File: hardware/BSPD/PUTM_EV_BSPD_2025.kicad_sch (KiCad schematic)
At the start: 37 parts, among them J1 BS2, J2 BS1, J3 CS, K2 TE AXICOM IM07DTS, Q1 BS170F, U10 LM393B, U11 74HC1G08GV, U5 74HC1G08GV, U6 74HC3G14, U8 NE555DR

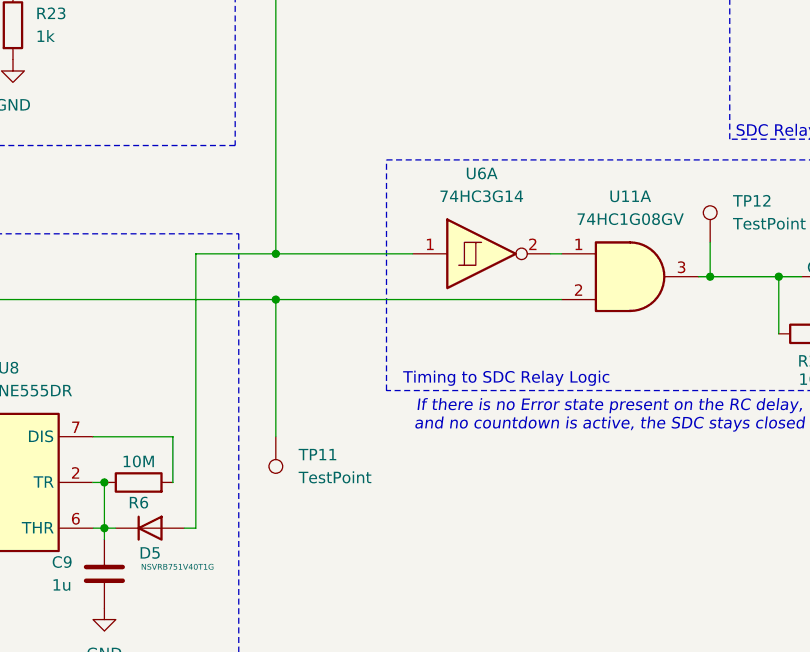
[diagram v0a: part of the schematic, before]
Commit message: Minor changes + reassigned inverters
Inverters changed to 2 dual packaged, since one more inverter appeared, and there was no quad inverter from chosen series.
Placed TestPoints more sensically
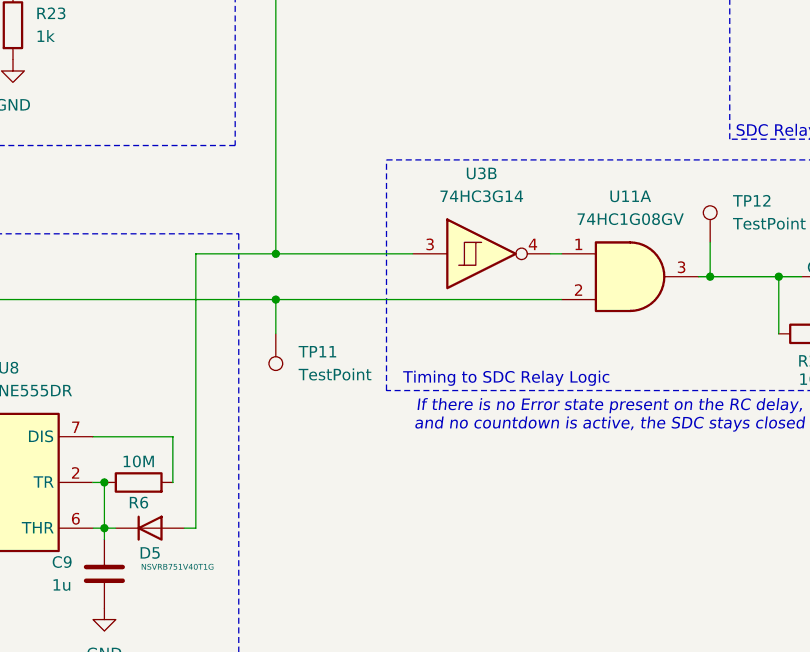
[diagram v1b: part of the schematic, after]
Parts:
- renumbered U6 to U3
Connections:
- net at D5.2 (A), R4.2, TP10.1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: now also U3.3; no longer U3.1
- net at U11.1: now also U3.4; no longer U3.2
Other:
- moved on the sheet: TP11
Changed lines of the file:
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@@
 	(wire
 		(pts
-			(xy 173.99 116.84) (xy 173.99 101.6)
+			(xy 173.99 105.41) (xy 173.99 101.6)
 		)
 		(stroke
@@
 		(lib_id "74xx:74HC14")
 		(at 196.85 96.52 0)
-		(unit 1)
+		(unit 2)
 		(exclude_from_sim no)
 		(in_bom yes)
@@
 		(dnp no)
 		(fields_autoplaced yes)
-		(property "Reference" "U6"
+		(property "Reference" "U3"
 			(at 196.85 87.63 0)
 			(effects
@@
 			(project ""
 				(path "/b652b05a-4e3d-4ad1-b032-18886abe7d45"
-					(reference "U6")
-					(unit 1)
+					(reference "U3")
+					(unit 2)
 				)
 			)
@@
 	(symbol
 		(lib_id "Connector:TestPoint")
-		(at 173.99 116.84 180)
+		(at 173.99 105.41 180)
 		(unit 1)
 		(exclude_from_sim no)
@@
 		(fields_autoplaced yes)
 		(property "Reference" "TP11"
-			(at 176.53 118.8719 0)
+			(at 176.53 107.4419 0)
 			(effects
 				(font
@@
 		)
 		(property "Value" "TestPoint"
-			(at 176.53 121.4119 0)
+			(at 176.53 109.9819 0)
 			(effects
 				(font
@@
 		)
 		(property "Footprint" ""
-			(at 168.91 116.84 0)
+			(at 168.91 105.41 0)
 			(effects
 				(font
@@
 		)
 		(property "Datasheet" "~"
-			(at 168.91 116.84 0)
+			(at 168.91 105.41 0)
 			(effects
 				(font
@@
 		)
 		(property "Description" "test point"
-			(at 173.99 116.84 0)
+			(at 173.99 105.41 0)
 			(effects
 				(font

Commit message: Assigned footprints
Harwin connectors not yet assigned!
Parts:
- C16, C17, C18, C7, C8, C9: footprint (none) -> Capacitor_SMD:C_0603_1608Metric
- D1: footprint (none) -> Diode_SMD:D_SMA
- D5: footprint (none) -> Diode_SMD:D_SOD-323_HandSoldering
- Q1: footprint (none) -> Package_TO_SOT_SMD:SOT-23
- R18, R19, R20, R22, R23, R4, R6: footprint (none) -> Resistor_SMD:R_0603_1608Metric
- U10: footprint (none) -> Package_SO:VSSOP-8_3x3mm_P0.65mm
- U11, U5: footprint (none) -> Package_TO_SOT_SMD:SOT-23-5
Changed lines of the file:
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@@
 			)
 		)
-		(property "Footprint" ""
+		(property "Footprint" "Resistor_SMD:R_0603_1608Metric"
 			(at 143.002 52.07 90)
 			(effects
@@
 			)
 		)
-		(property "Footprint" ""
+		(property "Footprint" "Resistor_SMD:R_0603_1608Metric"
 			(at 233.68 107.188 90)
 			(effects
@@
 			)
 		)
-		(property "Footprint" ""
+		(property "Footprint" "Capacitor_SMD:C_0603_1608Metric"
 			(at 82.55 177.8 0)
 			(effects
@@
 			)
 		)
-		(property "Footprint" ""
+		(property "Footprint" "Resistor_SMD:R_0603_1608Metric"
 			(at 143.002 71.12 90)
 			(effects
@@
 			)
 		)
-		(property "Footprint" ""
+		(property "Footprint" "Resistor_SMD:R_0603_1608Metric"
 			(at 134.112 66.04 90)
 			(effects
@@
 			)
 		)
-		(property "Footprint" ""
+		(property "Footprint" "Resistor_SMD:R_0603_1608Metric"
 			(at 116.84 61.468 90)
 			(effects
@@
 			)
 		)
-		(property "Footprint" ""
+		(property "Footprint" "Capacitor_SMD:C_0603_1608Metric"
 			(at 155.9052 135.89 0)
 			(effects
@@
 			)
 		)
-		(property "Footprint" ""
+		(property "Footprint" "Diode_SMD:D_SOD-323_HandSoldering"
 			(at 160.02 127 0)
 			(effects
@@
 			)
 		)
-		(property "Footprint" ""
+		(property "Footprint" "Package_SO:VSSOP-8_3x3mm_P0.65mm"
 			(at 156.21 62.23 0)
 			(effects
@@
 			)
 		)
-		(property "Footprint" ""
+		(property "Footprint" "Package_SO:VSSOP-8_3x3mm_P0.65mm"
 			(at 66.04 176.53 0)
 			(effects
@@
 			)
 		)
-		(property "Footprint" ""
+		(property "Footprint" "Resistor_SMD:R_0603_1608Metric"
 			(at 158.75 123.698 90)
 			(effects
@@
 			)
 		)
-		(property "Footprint" ""
+		(property "Footprint" "Resistor_SMD:R_0603_1608Metric"
 			(at 172.212 52.07 90)
 			(effects
@@
 			)
 		)
-		(property "Footprint" ""
+		(property "Footprint" "Package_TO_SOT_SMD:SOT-23"
 			(at 242.57 96.52 0)
 			(effects
@@
 			)
 		)
-		(property "Footprint" ""
+		(property "Footprint" "Package_TO_SOT_SMD:SOT-23-5"
 			(at 213.36 99.06 0)
 			(effects
@@
 			)
 		)
-		(property "Footprint" ""
+		(property "Footprint" "Package_TO_SOT_SMD:SOT-23-5"
 			(at 34.29 176.53 0)
 			(effects
@@
 			)
 		)
-		(property "Footprint" ""
+		(property "Footprint" "Package_TO_SOT_SMD:SOT-23-5"
 			(at 80.01 96.52 0)
 			(effects
@@
 			)
 		)
-		(property "Footprint" ""
+		(property "Footprint" "Package_TO_SOT_SMD:SOT-23-5"
 			(at 90.17 177.8 0)
 			(effects
@@
 			)
 		)
-		(property "Footprint" ""
+		(property "Footprint" "Capacitor_SMD:C_0603_1608Metric"
 			(at 68.58 176.53 0)
 			(effects
@@
 			)
 		)
-		(property "Footprint" ""
+		(property "Footprint" "Capacitor_SMD:C_0603_1608Metric"
 			(at 129.2352 135.89 0)
 			(effects
@@
 			)
 		)
-		(property "Footprint" ""
+		(property "Footprint" "Diode_SMD:D_SMA"
 			(at 255.27 77.47 0)
 			(effects
@@
 			)
 		)
-		(property "Footprint" ""
+		(property "Footprint" "Capacitor_SMD:C_0603_1608Metric"
 			(at 26.67 176.53 0)
 			(effects
@@
 			)
 		)
-		(property "Footprint" ""
+		(property "Footprint" "Capacitor_SMD:C_0603_1608Metric"
 			(at 131.7752 69.85 0)
 			(effects

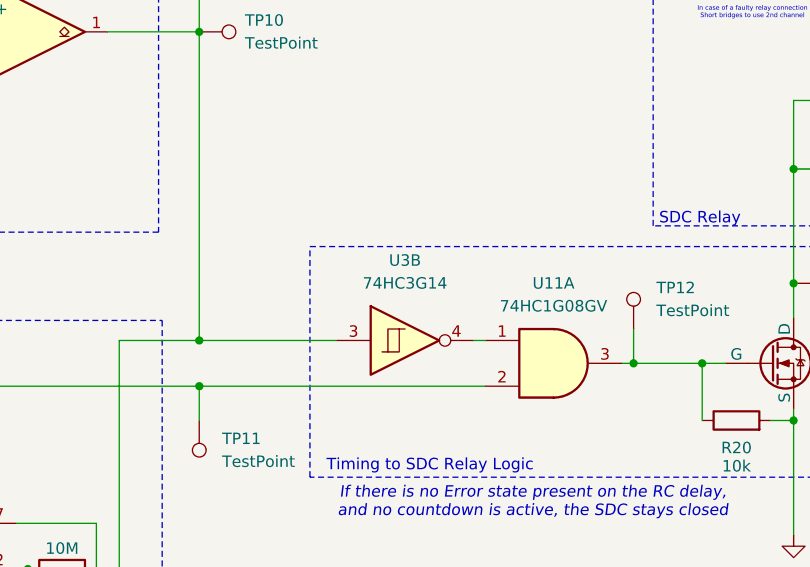
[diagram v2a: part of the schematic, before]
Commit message: Fixed misassigned U3 value + power
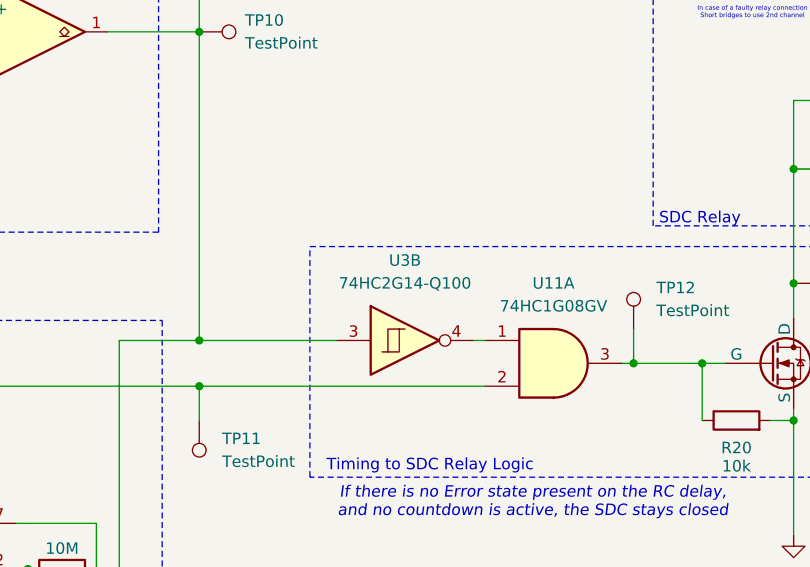
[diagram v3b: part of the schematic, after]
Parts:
- U3: value 74HC3G14 -> 74HC2G14-Q100; footprint (none) -> Package_TO_SOT_SMD:SOT-23-6
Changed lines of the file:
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@@
 			)
 		)
-		(property "Value" "74HC3G14"
+		(property "Value" "74HC2G14-Q100"
 			(at 196.85 90.17 0)
 			(effects
@@
 			)
 		)
-		(property "Footprint" ""
+		(property "Footprint" "Package_TO_SOT_SMD:SOT-23-6"
 			(at 196.85 96.52 0)
 			(effects

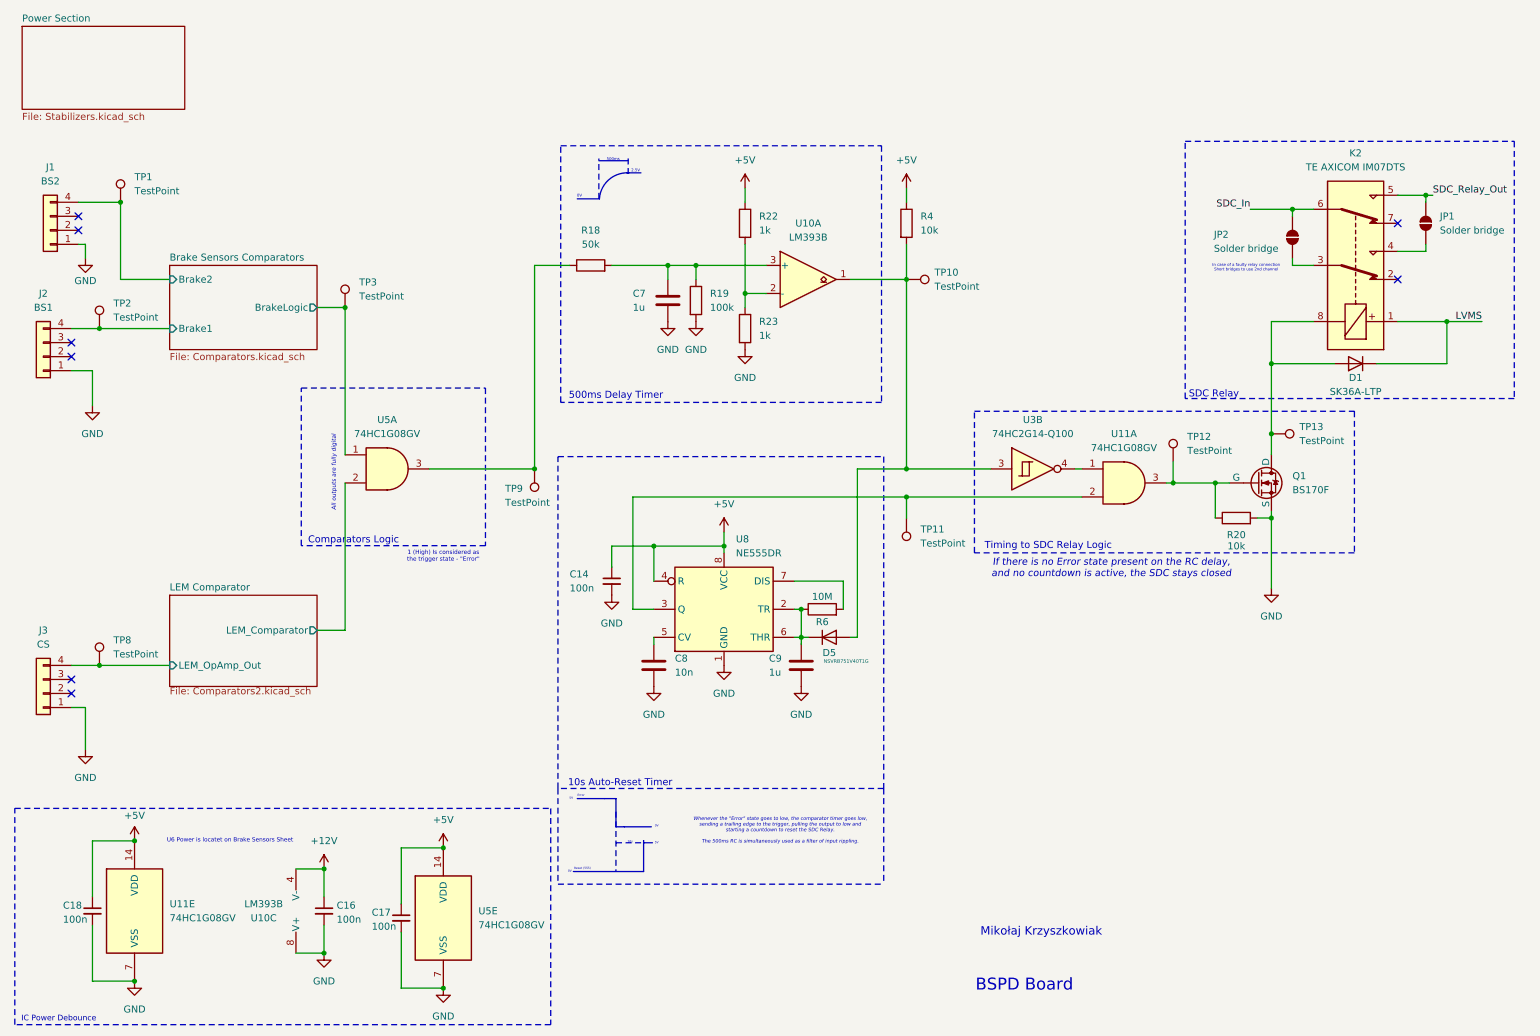
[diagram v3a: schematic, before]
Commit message: Fixed symbol errors
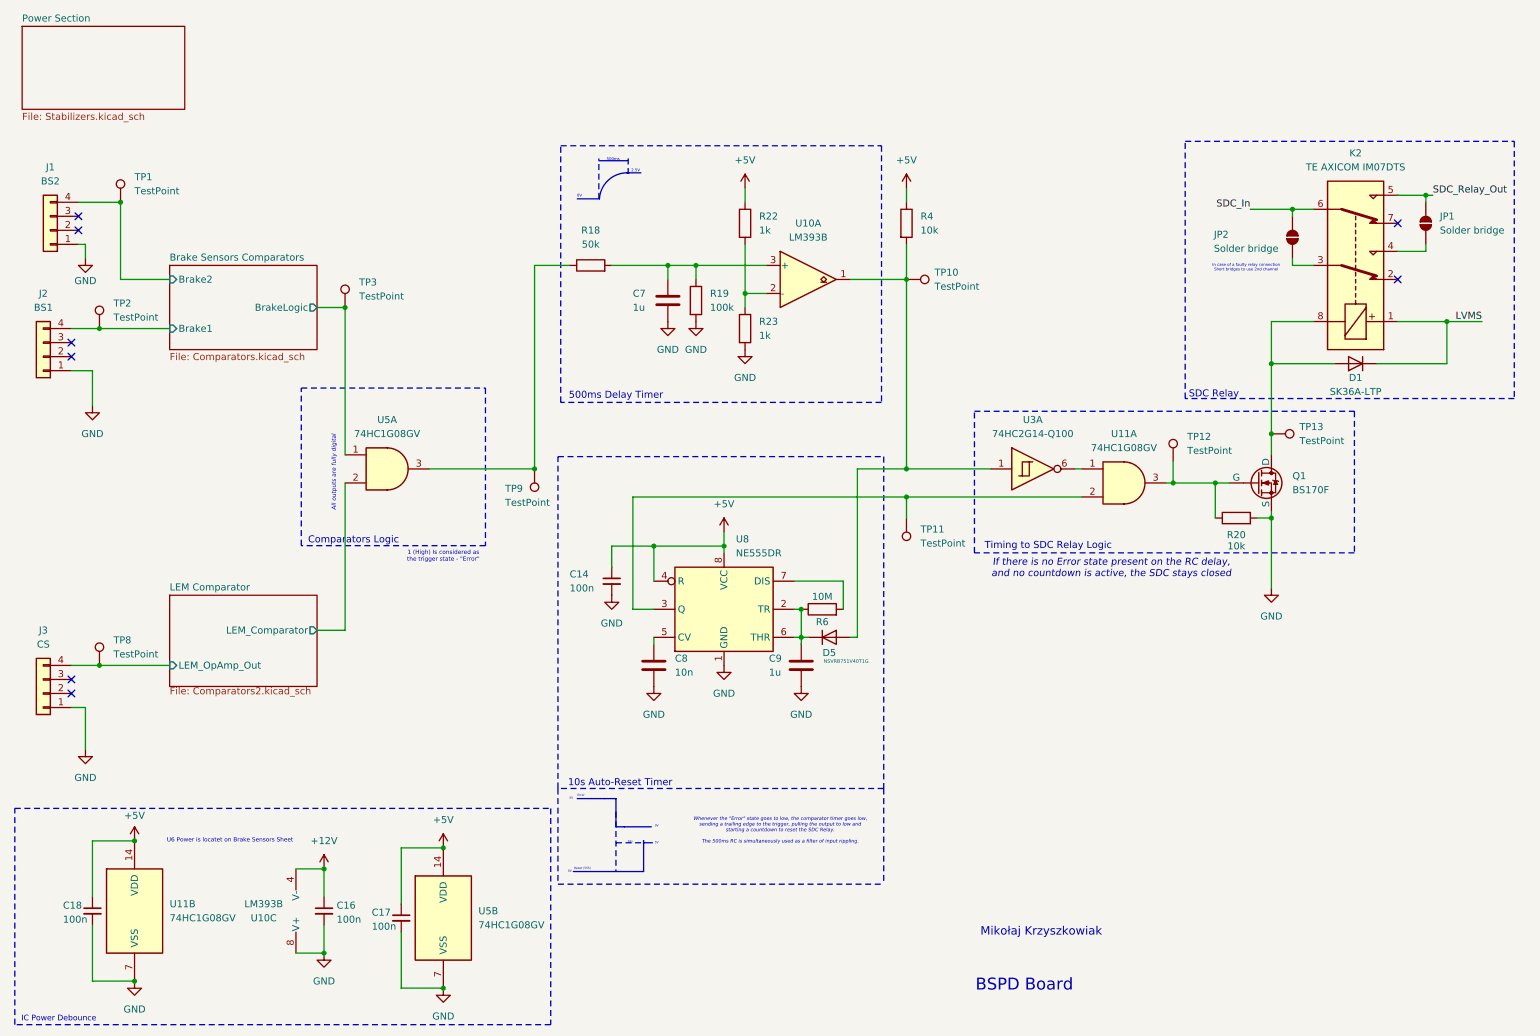
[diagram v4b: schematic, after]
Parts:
- removed unit 5 of U11
- removed U3: 74HC2G14-Q100, Package_TO_SOT_SMD:SOT-23-6, symbol 74xx:74HC14
- added U3: 74HC2G14-Q100, Package_SO:TSOP-6_1.65x3.05mm_P0.95mm, symbol 74HC:Inv_Schmitt
- U10: footprint Package_SO:VSSOP-8_3x3mm_P0.65mm -> Package_SO:TSSOP-8_3x3mm_P0.65mm
- U11, U5: footprint Package_TO_SOT_SMD:SOT-23-5 -> Package_TO_SOT_SMD:SC-74A-5_1.55x2.9mm_P0.95mm
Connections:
- net +5V: now also U11.14 (VDD), U5.14 (VDD); no longer U5.14 (VDD)
- net GND: now also U11.7 (VSS), U5.7 (VSS); no longer U5.7 (VSS)
- net at D5.2 (A), R4.2, TP10.1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: now also U3.1
- net at U11.1: now also U3.6
